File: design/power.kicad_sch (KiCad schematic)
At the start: 13 parts

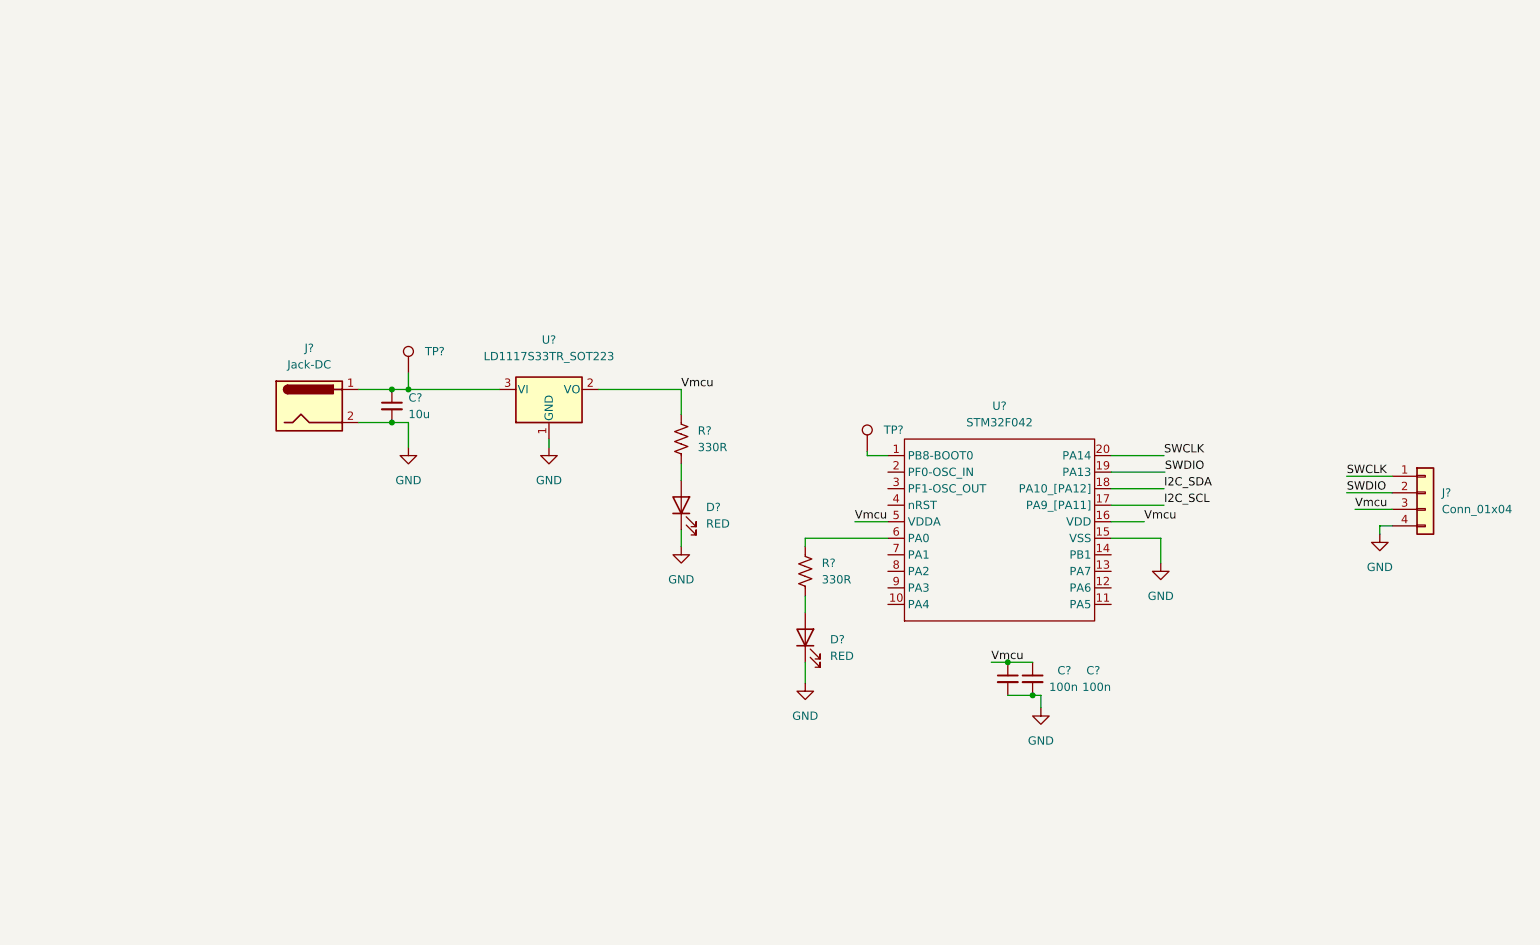
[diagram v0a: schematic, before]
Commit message: schematic: start pmic
Signed-off-by: Zbigniew Opiol <zbigniew.opiol@tbs-biometrics.com>
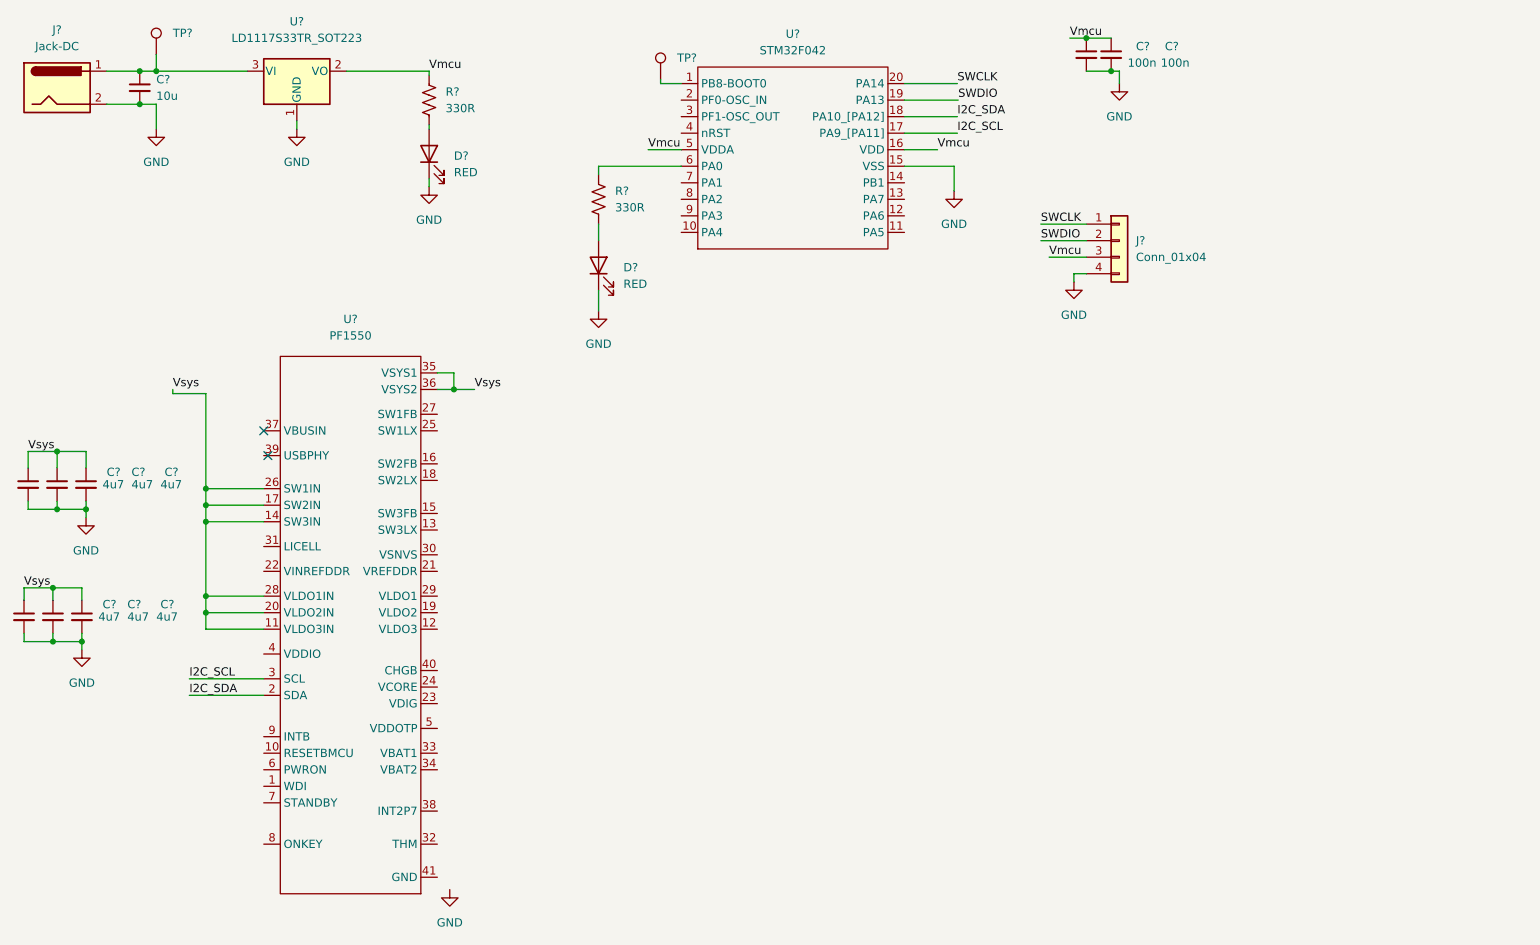
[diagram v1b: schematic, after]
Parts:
- added C? (x6): 4u7, Capacitor_SMD:C_0805_2012Metric_Pad1.18x1.45mm_HandSolder, symbol Device:C_Small
- added U?: PF1550, Package_DFN_QFN:QFN-40-1EP_5x5mm_P0.4mm_EP3.6x3.6mm_ThermalVias, symbol zbop:PF1550
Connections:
- net GND: now also C?.2, C?.2, C?.2, C?.2, C?.2, C?.2
- net I2C_SCL: now also U?.3 (SCL)
- net I2C_SDA: now also U?.2 (SDA)
- new net Vsys: C?.1, C?.1, C?.1, C?.1, C?.1, C?.1, U?.11 (VLDO3IN), U?.14 (SW3IN), U?.17 (SW2IN), U?.20 (VLDO2IN), U?.26 (SW1IN), U?.28 (VLDO1IN), U?.35 (VSYS1), U?.36 (VSYS2)
- no-connect marks 0 -> 2
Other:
- moved on the sheet: C?, D?, J?, R?, TP?, U?
